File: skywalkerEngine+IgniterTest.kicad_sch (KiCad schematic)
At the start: 49 parts

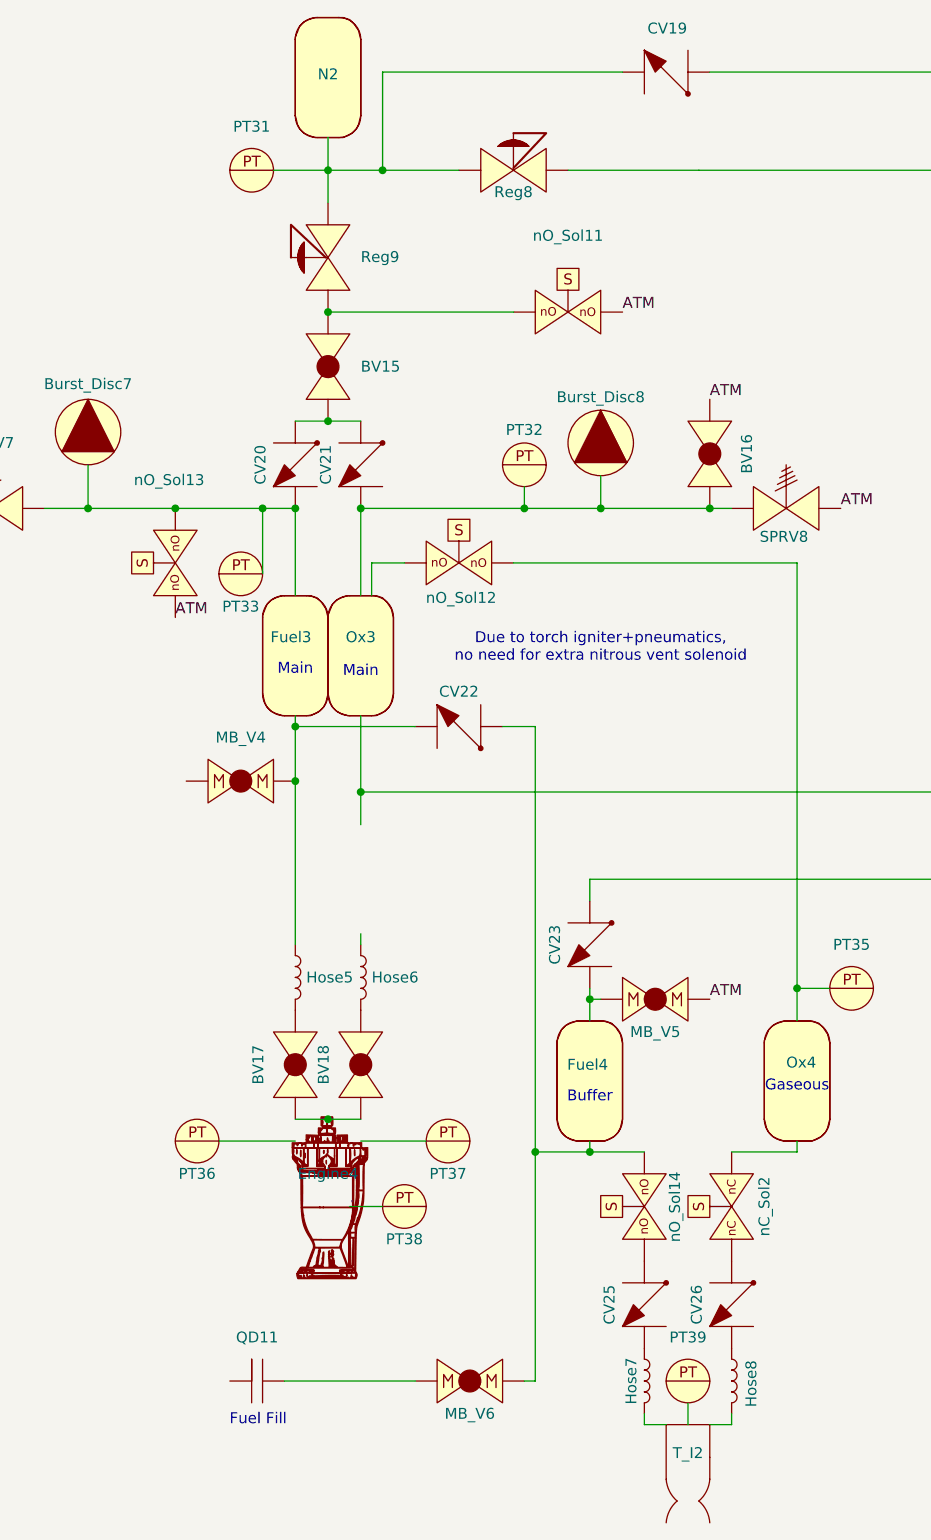
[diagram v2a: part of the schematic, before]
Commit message: Modified Hopper Eng test
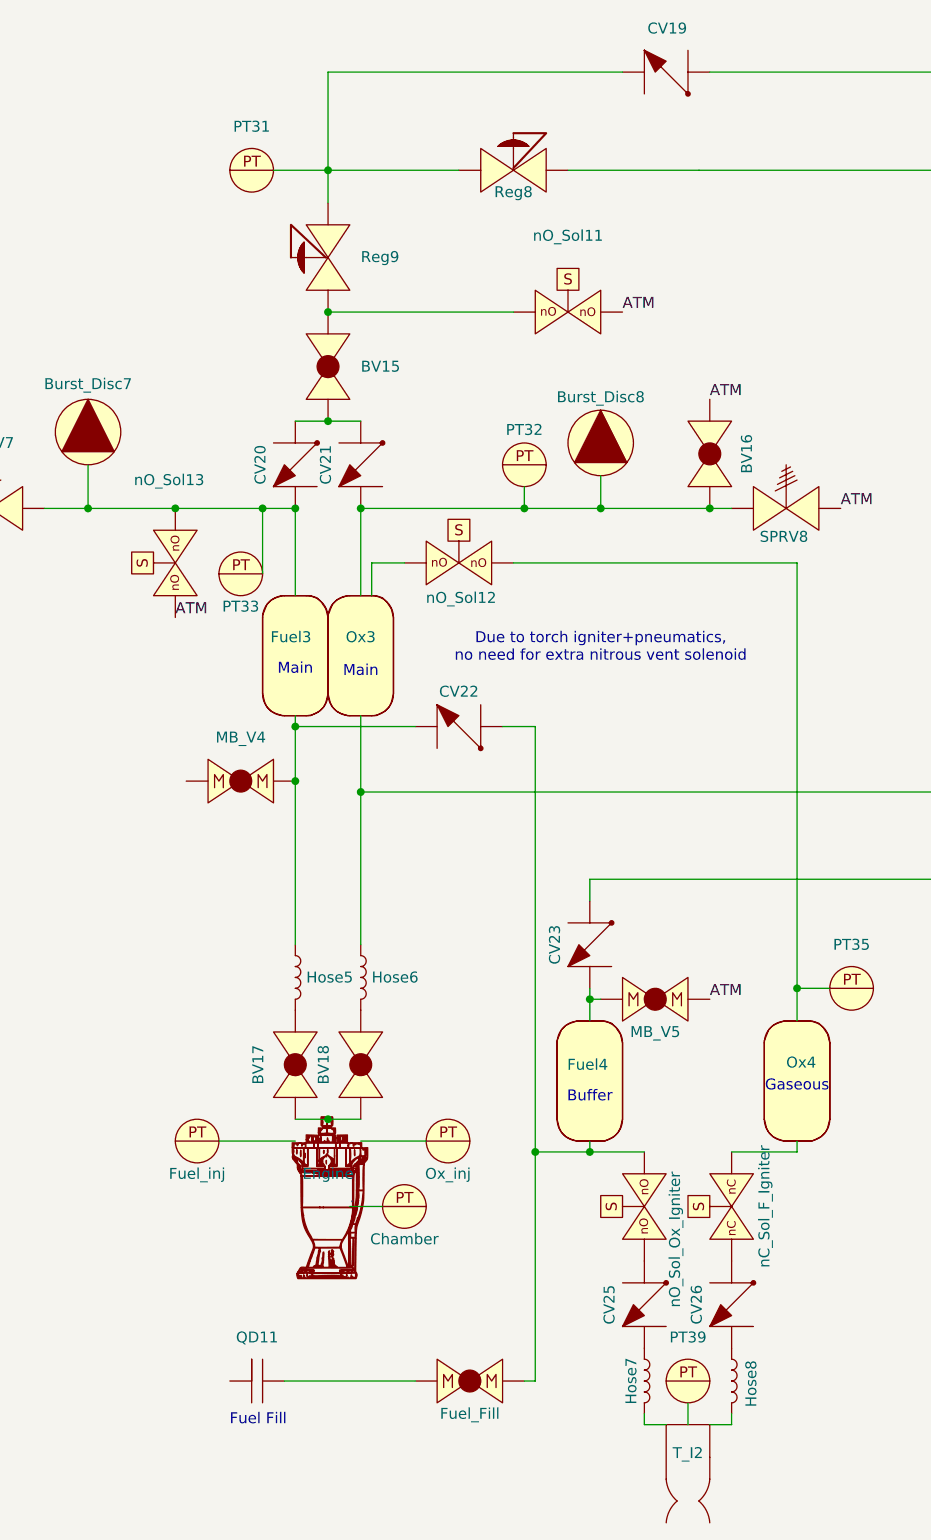
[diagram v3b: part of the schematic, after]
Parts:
- removed N2: ~, symbol PID_symbols:Tank
- renumbered PT38 to Chamber, Engine4 to Engine, MB_V6 to Fuel_Fill, PT36 to Fuel_inj, PT37 to Ox_inj, nC_Sol2 to nC_Sol_F_Igniter, nO_Sol14 to nO_Sol_Ox_Igniter
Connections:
- net at Fuel_inj.: now also Engine.
- net at Engine.: now also Ox_inj.; no longer Fuel_inj.
- net at CV25.: now also Hose7.1; no longer nO_Sol_Ox_Igniter.
- net at MB_V4.: now also CV22., Fuel3., Hose5.1
- net at QD9.: now also CV24.
- net at CV24.: now also Hose6.1, Ox3.; no longer QD9.
- net at PT31.: now also CV19., Reg8., Reg9.
- net at Ox_inj.: no longer Engine.
- new net: Burst_Disc7., CV20., Fuel3., PT33., SPRV7., nO_Sol13.
- new net: Ox4., PT35., nO_Sol12.
- new net: CV25., nO_Sol_Ox_Igniter.
- new net: CV23., PT34., Reg8.
- new net: CV23., Fuel4., MB_V5.
- new net: BV17., BV18., Engine.
- new net: BV16., Burst_Disc8., CV21., Ox3., PT32., SPRV8.
- new net: BV15., Reg9., nO_Sol11.
- now unconnected: Burst_Disc7., Burst_Disc8., PT32., PT33., PT34., PT35.
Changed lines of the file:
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@@
 	)
 	(junction
-		(at 71.12 38.1)
-		(diameter 0)
-		(color 0 0 0 0)
-	)
-	(junction
 		(at 119.38 133.35)
 		(diameter 0)
@@
 	(wire
 		(pts
-			(xy 71.12 26.67) (xy 99.06 26.67)
+			(xy 64.77 26.67) (xy 99.06 26.67)
 		)
 		(stroke
@@
 	(wire
 		(pts
-			(xy 71.12 38.1) (xy 71.12 26.67)
+			(xy 64.77 38.1) (xy 64.77 26.67)
 		)
 		(stroke
@@
 	(wire
 		(pts
-			(xy 68.58 128.27) (xy 68.58 127)
-		)
-		(stroke
-			(width 0)
-			(type default)
-		)
-	)
-	(wire
-		(pts
 			(xy 85.09 102.87) (xy 88.9 102.87)
 		)
@@
 	(wire
 		(pts
-			(xy 71.12 38.1) (xy 80.01 38.1)
-		)
-		(stroke
-			(width 0)
-			(type default)
-		)
-	)
-	(wire
-		(pts
 			(xy 69.85 83.82) (xy 69.85 87.63)
 		)
@@
 	(wire
 		(pts
-			(xy 68.58 110.49) (xy 68.58 114.3)
-		)
-		(stroke
-			(width 0)
-			(type default)
-		)
-	)
-	(wire
-		(pts
 			(xy 60.96 148.59) (xy 64.77 148.59)
 		)
@@
 	(wire
 		(pts
-			(xy 64.77 38.1) (xy 71.12 38.1)
+			(xy 64.77 38.1) (xy 80.01 38.1)
 		)
 		(stroke
@@
 	(wire
 		(pts
-			(xy 64.77 38.1) (xy 64.77 34.29)
+			(xy 87.63 77.47) (xy 96.52 77.47)
 		)
 		(stroke
@@
 	(wire
 		(pts
-			(xy 87.63 77.47) (xy 96.52 77.47)
+			(xy 68.58 110.49) (xy 68.58 128.27)
 		)
 		(stroke
@@
 		(on_board yes)
 		(dnp no)
-		(property "Reference" "PT36"
+		(property "Reference" "Fuel_inj"
 			(at 49.53 154.94 0)
 			(effects
@@
 			(project "P_IDs"
 				(path "/045f1f05-3134-4b6d-91b6-463031104f1e/e56eb7fc-ceaa-4516-b7d6-446a7aeba6c0"
-					(reference "PT36")
+					(reference "Fuel_inj")
 					(unit 1)
 				)
@@
 		(on_board yes)
 		(dnp no)
-		(property "Reference" "PT38"
+		(property "Reference" "Chamber"
 			(at 73.66 162.56 0)
 			(effects
@@
 			(project "P_IDs"
 				(path "/045f1f05-3134-4b6d-91b6-463031104f1e/e56eb7fc-ceaa-4516-b7d6-446a7aeba6c0"
-					(reference "PT38")
+					(reference "Chamber")
 					(unit 1)
 				)
@@
 		(on_board yes)
 		(dnp no)
-		(property "Reference" "MB_V6"
+		(property "Reference" "Fuel_Fill"
 			(at 81.28 182.88 0)
 			(effects
@@
 			(project "P_IDs"
 				(path "/045f1f05-3134-4b6d-91b6-463031104f1e/e56eb7fc-ceaa-4516-b7d6-446a7aeba6c0"
-					(reference "MB_V6")
+					(reference "Fuel_Fill")
 					(unit 1)
 				)
@@
 		(on_board yes)
 		(dnp no)
-		(property "Reference" "nO_Sol14"
+		(property "Reference" "nO_Sol_Ox_Igniter"
 			(at 105.156 154.686 0)
 			(effects
@@
 			(project "P_IDs"
 				(path "/045f1f05-3134-4b6d-91b6-463031104f1e/e56eb7fc-ceaa-4516-b7d6-446a7aeba6c0"
-					(reference "nO_Sol14")
+					(reference "nO_Sol_Ox_Igniter")
 					(unit 1)
 				)
@@
 		(on_board yes)
 		(dnp no)
-		(property "Reference" "nC_Sol2"
+		(property "Reference" "nC_Sol_F_Igniter"
 			(at 115.57 158.75 0)
 			(effects
@@
 			(project "P_IDs"
 				(path "/045f1f05-3134-4b6d-91b6-463031104f1e/e56eb7fc-ceaa-4516-b7d6-446a7aeba6c0"
-					(reference "nC_Sol2")
+					(reference "nC_Sol_F_Igniter")
 					(unit 1)
 				)
@@
 		(on_board yes)
 		(dnp no)
-		(property "Reference" "Engine4"
+		(property "Reference" "Engine"
 			(at 64.77 154.94 0)
 			(effects
@@
 			(project "P_IDs"
 				(path "/045f1f05-3134-4b6d-91b6-463031104f1e/e56eb7fc-ceaa-4516-b7d6-446a7aeba6c0"
-					(reference "Engine4")
+					(reference "Engine")
 					(unit 1)
 				)
@@
 		(on_board yes)
 		(dnp no)
-		(property "Reference" "PT37"
+		(property "Reference" "Ox_inj"
 			(at 78.74 154.94 0)
 			(effects
@@
 			(project "P_IDs"
 				(path "/045f1f05-3134-4b6d-91b6-463031104f1e/e56eb7fc-ceaa-4516-b7d6-446a7aeba6c0"
-					(reference "PT37")
+					(reference "Ox_inj")
 					(unit 1)
 				)
@@
 					(unit 1)
 				)
-			)
-		)
-	)
-	(symbol
-		(lib_name "PID_symbols:Tank")
-		(lib_id "PID_symbols:Tank")
-		(at 63.5 31.75 0)
-		(unit 1)
-		(exclude_from_sim no)
-		(in_bom yes)
-		(on_board yes)
-		(dnp no)
-		(property "Reference" "N2"
-			(at 64.77 26.924 0)
-			(effects
-				(font
-					(size 1.27 1.27)
-				)
-			)
-		)
-		(property "Value" "~"
-			(at 63.5 31.75 0)
-			(effects
-				(font
-					(size 1.27 1.27)
-				)
-			)
-		)
-		(property "Footprint" ""
-			(at 63.5 31.75 0)
-			(effects
-				(font
-					(size 1.27 1.27)
-				)
-				(hide yes)
-			)
-		)
-		(property "Datasheet" ""
-			(at 63.5 31.75 0)
-			(effects
-				(font
-					(size 1.27 1.27)
-				)
-				(hide yes)
-			)
-		)
-		(property "Description" ""
-			(at 63.5 31.75 0)
-			(effects
-				(font
-					(size 1.27 1.27)
-				)
-				(hide yes)
-			)
-		)
-		(pin ""
-		)
-		(pin ""
-		)
-		(instances
-			(project "P_IDs"
-				(path "/045f1f05-3134-4b6d-91b6-463031104f1e/e56eb7fc-ceaa-4516-b7d6-446a7aeba6c0"
-					(reference "N2")
-					(unit 1)
-				)

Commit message: overwrite
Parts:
- removed BV15: ~, symbol PID_symbols:Ball_Valve
- removed CV24: ~, symbol PID_symbols:Check_Valve
- removed QD10, QD9: ~, symbol PID_symbols:Quick_Disconnect
- added CV?: ~, symbol PID_symbols:Check_Valve
- added Hose?: ~, symbol Device:Hose
- added N2_Bottl;e, Ox_Bottle: ~, symbol PID_symbols:Tank
- added N2_Press, N2_Press?: ~, symbol PID_symbols:Ball_Valve
- added PT?: ~, symbol PID_symbols:Pressure_Transducer
- added nO_Sol?: ~, symbol PID_symbols:Normally Open Solenoid
- renumbered PT33 to Fuel_Tank, PT31 to N2_Hose, PT34 to N2_Pn, PT35 to Ox_Buffer, PT32 to Ox_Tank
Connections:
- net ATM: now also nO_Sol?.
- net at Fuel_inj.: now also Engine.
- net at Engine.: now also Ox_inj.; no longer Fuel_inj.
- net at CV25.: now also Hose7.1; no longer nO_Sol_Ox_Igniter.
- net at CV20., CV21.: now also Reg9., nO_Sol11.
- net at MB_V4.: now also CV22., Fuel3., Hose5.1
- net at Reg9.: now also CV19., N2_Hose., Reg8.; no longer nO_Sol11.
- net at Hose6.1, Ox3.: now also CV?.
- net at Ox_inj.: no longer Engine.
- net at CV19.: now also N2_Press.
- new net: Burst_Disc7., CV20., Fuel3., Fuel_Tank., SPRV7., nO_Sol13.
- new net: Ox4., Ox_Buffer., nO_Sol12.
- new net: CV25., nO_Sol_Ox_Igniter.
- new net: CV23., N2_Pn., Reg8.
- new net: CV23., Fuel4., MB_V5.
- new net: Hose?.1, N2_Press., PT?.
- new net: BV17., BV18., Engine.
- new net: BV16., Burst_Disc8., CV21., Ox3., Ox_Tank., SPRV8., nO_Sol?.
- new net: N2_Press?., Ox_Bottle.
- new net: Hose?.2, N2_Bottl;e.
- new net: CV?., N2_Press?.
- now unconnected: Burst_Disc7., Burst_Disc8., Fuel_Tank., N2_Pn., Ox_Buffer., Ox_Tank.
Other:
- note removed: "Nitrous Fill"
- moved on the sheet: BV16, Fuel_Tank, SPRV8

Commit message: no message
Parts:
- removed BV16, BV17, BV18, N2_Press, N2_Press?: ~, symbol PID_symbols:Ball_Valve
- removed Burst_Disc7, Burst_Disc8: ~, symbol PID_symbols:Burst_Disc
- removed CV19, CV20, CV21, CV22, CV23, CV25, CV26, CV?: ~, symbol PID_symbols:Check_Valve
- removed Chamber, Fuel_Tank, Fuel_inj, N2_Hose, N2_Pn, Ox_Buffer, Ox_Tank, Ox_inj, PT39, PT?: ~, symbol PID_symbols:Pressure_Transducer
- removed Engine: ~, symbol PID_symbols:Engine
- removed Fuel3, Fuel4, N2_Bottl;e, Ox3, Ox4, Ox_Bottle: ~, symbol PID_symbols:Tank
- removed Fuel_Fill, MB_V4, MB_V5: ~, symbol PID_symbols:MBallValve
- removed Hose5, Hose6, Hose7, Hose8, Hose?: ~, symbol Device:Hose
- removed QD11: ~, symbol PID_symbols:Quick_Disconnect
- removed Reg8, Reg9: ~, symbol PID_symbols:Pressure_Regulator
- removed SPRV7, SPRV8: ~, symbol PID_symbols:SPRV
- removed T_I2: ~, symbol Analog_ADC:Torch_Igniter
- removed nC_Sol_F_Igniter: ~, symbol PID_symbols:Normally_Closed_Solenoid
- removed nO_Sol11, nO_Sol12, nO_Sol13, nO_Sol_Ox_Igniter: ~, symbol PID_symbols:Solenoid
- removed nO_Sol?: ~, symbol PID_symbols:Normally Open Solenoid
- added BV? (x6): ~, symbol PID_symbols:Ball_Valve
- added Burst_Disc?: ~, symbol PID_symbols:Burst_Disc
- added CV? (x3): ~, symbol PID_symbols:Check_Valve
- added Engine?: ~, symbol PID_symbols:Engine
- added Hose? (x2): ~, symbol Device:Hose
- added PT? (x7): ~, symbol PID_symbols:Pressure_Transducer
- added Pmatic_B_Valve?: ~, symbol PID_symbols:Pneumatic_Rotary_Ball_Valve
- added Reg? (x2): ~, symbol PID_symbols:Pressure_Regulator
- added SPRV?: ~, symbol PID_symbols:SPRV
- added T? (x6): ~, symbol PID_symbols:Tank
- added nO_Sol? (x3): ~, symbol PID_symbols:Solenoid
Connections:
- net .: now also PT?.
- new net: BV?., Engine?., PT?. (x2)
- new net: Reg?., T?.
- new net: BV?., Pmatic_B_Valve?.
- new net: BV?., CV?., PT?., T?.
- new net: CV?., Hose?.2
- new net: Hose?.1, T?.
- new net: BV?., Burst_Disc?., CV?., CV?., SPRV?.
- new net: BV?., Reg?.
- new net: T?., nO_Sol?.
- new net: BV?., CV?., T?., nO_Sol?.
- new net: BV?., T?.
- new net: Hose?.2, PT?., Reg?., Reg?.
- new net: PT?., Pmatic_B_Valve?., T?.
- new net: BV?., Hose?.1
- new net: BV?., CV?., nO_Sol?.
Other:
- note removed: "Buffer"
- note removed: "Due to torch igniter+pneumatics, no need for extra nitrous vent solenoid"
- note removed: "Fuel Fill"
- note removed: "Gaseous"
- note removed: "Main"

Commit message: no message
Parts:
- removed Pmatic_B_Valve?: ~, symbol PID_symbols:Pneumatic_Rotary_Ball_Valve
- added CV? (x3): ~, symbol PID_symbols:Check_Valve
- added Hose? (x2): ~, symbol Device:Hose
- added MB_V? (x2): ~, symbol PID_symbols:MBallValve
- added PT?: ~, symbol PID_symbols:Pressure_Transducer
- added QD?: ~, symbol PID_symbols:Quick_Disconnect
- added T_I?: ~, symbol Analog_ADC:Torch_Igniter
- added nC_Sol?: ~, symbol PID_symbols:Normally_Closed_Solenoid
- added nO_Sol?: ~, symbol PID_symbols:Normally Open Solenoid
- gave numbers to parts that had none: 2
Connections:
- net at Engine?.: now also BV?., PT?.
- net at Eth_Buff.: now also BV?., PT?., T?., MB_V?., nO_Sol?.
- net at Reg?.: now also CV?.; no longer Eth_Buff.
- net at T?.: now also Hose?.1
- net at nO_Sol?.: now also Ox_Buffer.
- net at BV?.: now also CV?., T?., nO_Sol?.
- net at T?.: now also BV?.
- net at BV?.: now also Hose?.1; no longer T?.
- net at PT?.: no longer T?.
- net at BV?.: now also CV?., nO_Sol?.
- new net: BV?., Engine?., PT?.
- new net: CV?., Eth_Buff., MB_V?.
- new net: CV?., nC_Sol?.
- new net: Ox_Buffer., nC_Sol?.
- new net: BV?., CV?., PT?., T?.
- new net: BV?., Burst_Disc?., CV?., CV?., SPRV?.
- new net: CV?., Hose?.1
- new net: Hose?.2, T_I?.
- new net: CV?., nO_Sol?.
- new net: CV?., Hose?.2
- new net: MB_V?., QD?.
- new net: Hose?.1, T_I?.
- now unconnected: Burst_Disc?., PT?., PT?., PT?., SPRV?., nO_Sol?., nO_Sol?.
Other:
- moved on the sheet: BV?, Engine?, Eth_Buff, Ox_Buffer, PT?

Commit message: no message
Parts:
- added CV?: ~, symbol PID_symbols:Check_Valve
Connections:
- net at Engine?.: now also BV?., PT?.
- net at nC_Sol?.: now also Ox_Buffer.; no longer CV?.
- net at Ox_Buffer.: now also nO_Sol?.; no longer nC_Sol?.
- net at T?.: now also Hose?.1
- net at BV?.: now also CV?., T?., nO_Sol?.
- net at T?.: now also BV?.
- net at BV?.: now also Hose?.1; no longer T?.
- net at QD?.: now also MB_V?.
- net at BV?.: now also CV?., nO_Sol?.
- new net: CV?., Eth_Buff., MB_V?., nO_Sol?.
- new net: BV?., CV?., PT?., T?. (x2)
- new net: BV?., Engine?., PT?.
- new net: CV?., Eth_Buff., MB_V?.
- new net: CV?., nC_Sol?.
- new net: BV?., Burst_Disc?., CV?., CV?., SPRV?.
- now unconnected: Burst_Disc?., MB_V?., PT?., PT?., PT?., PT?., SPRV?., T?., nO_Sol?., nO_Sol?.
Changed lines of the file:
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@@
+	(wire
+		(pts
+			(xy 186.69 91.44) (xy 186.69 102.87)
+		)
+		(stroke
+			(width 0.635)
+			(type default)
+		)
+	)
 	(wire
 		(pts
@@
 	(wire
 		(pts
-			(xy 186.69 73.66) (xy 186.69 102.87)
+			(xy 186.69 73.66) (xy 186.69 81.28)
 		)
 		(stroke
@@
 		)
 	)
+	(symbol
+		(lib_name "Check_Valve_3")
+		(lib_id "PID_symbols:Check_Valve")
+		(at 186.69 88.9 90)
+		(unit 1)
+		(exclude_from_sim no)
+		(in_bom yes)
+		(on_board yes)
+		(dnp no)
+		(fields_autoplaced yes)
+		(property "Reference" "CV?"
+			(at 190.5 85.8519 90)
+			(effects
+				(font
+					(size 1.27 1.27)
+				)
+				(justify right)
+			)
+		)
+		(property "Value" "~"
+			(at 190.5 87.757 90)
+			(effects
+				(font
+					(size 1.27 1.27)
+				)
+				(justify right)
+			)
+		)
+		(property "Footprint" ""
+			(at 186.69 88.9 0)
+			(effects
+				(font
+					(size 1.27 1.27)
+				)
+				(hide yes)
+			)
+		)
+		(property "Datasheet" ""
+			(at 186.69 88.9 0)
+			(effects
+				(font
+					(size 1.27 1.27)
+				)
+				(hide yes)
+			)
+		)
+		(property "Description" ""
+			(at 186.69 88.9 0)
+			(effects
+				(font
+					(size 1.27 1.27)
+				)
+				(hide yes)
+			)
+		)
+		(pin ""
+		)
+		(pin ""
+		)
+		(instances
+			(project ""
+				(path "/045f1f05-3134-4b6d-91b6-463031104f1e/e56eb7fc-ceaa-4516-b7d6-446a7aeba6c0"
+					(reference "CV?")
+					(unit 1)
+				)
+			)
+		)
+	)

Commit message: no message
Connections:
- net at Engine?.: now also BV?., PT?.
- net at nC_Sol?.: now also Ox_Buffer.; no longer CV?.
- net at Ox_Buffer.: now also nO_Sol?.; no longer nC_Sol?.
- net at T?.: now also Hose?.1
- net at BV?.: now also CV?., T?., nO_Sol?.
- net at T?.: now also BV?.
- net at BV?.: now also Hose?.1; no longer T?.
- net at QD?.: now also MB_V?.
- net at BV?.: now also CV?., nO_Sol?.
- new net: CV?., Eth_Buff., MB_V?., nO_Sol?.
- new net: BV?., CV?., PT?., T?. (x2)
- new net: BV?., Engine?., PT?.
- new net: CV?., Eth_Buff., MB_V?.
- new net: CV?., nC_Sol?.
- new net: BV?., Burst_Disc?., CV?., CV?., SPRV?.
- now unconnected: Burst_Disc?., MB_V?., PT?., PT?., PT?., PT?., SPRV?., T?., nO_Sol?., nO_Sol?.
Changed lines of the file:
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@@
 	)
 	(symbol
-		(lib_name "PID_symbols:Ball_Valve")
 		(lib_id "PID_symbols:Ball_Valve")
 		(at 143.51 110.49 270)
@@
 	)
 	(symbol
-		(lib_name "PID_symbols:Check_Valve")
 		(lib_id "PID_symbols:Check_Valve")
 		(at 93.98 107.95 0)
@@
 	)
 	(symbol
-		(lib_name "PID_symbols:Tank")
 		(lib_id "PID_symbols:Tank")
 		(at 124.46 30.48 0)
@@
 	)
 	(symbol
-		(lib_name "PID_symbols:Ball_Valve")
 		(lib_id "PID_symbols:Ball_Valve")
 		(at 130.81 118.11 90)
@@
 	)
 	(symbol
-		(lib_name "PID_symbols:Pressure_Transducer")
 		(lib_id "PID_symbols:Pressure_Transducer")
 		(at 125.73 132.08 0)
@@
 	)
 	(symbol
-		(lib_name "PID_symbols:Ball_Valve")
 		(lib_id "PID_symbols:Ball_Valve")
 		(at 125.73 63.5 270)
@@
 	)
 	(symbol
-		(lib_name "PID_symbols:Pressure_Transducer")
 		(lib_id "PID_symbols:Pressure_Transducer")
 		(at 125.73 125.73 0)
@@
 	)
 	(symbol
-		(lib_name "PID_symbols:Pressure_Transducer")
 		(lib_id "PID_symbols:Pressure_Transducer")
 		(at 114.3 119.38 0)
@@
 	)
 	(symbol
-		(lib_name "PID_symbols:Solenoid")
 		(lib_id "PID_symbols:Solenoid")
 		(at 100.33 127 90)
@@
 	)
 	(symbol
-		(lib_name "PID_symbols:Check_Valve")
 		(lib_id "PID_symbols:Check_Valve")
 		(at 203.2 118.11 270)
@@
 	)
 	(symbol
-		(lib_name "PID_symbols:Pressure_Transducer")
 		(lib_id "PID_symbols:Pressure_Transducer")
 		(at 147.32 123.19 0)
@@
 	)
 	(symbol
-		(lib_name "PID_symbols:Ball_Valve")
 		(lib_id "PID_symbols:Ball_Valve")
 		(at 107.95 87.63 0)
@@
 	)
 	(symbol
-		(lib_name "PID_symbols:Tank")
 		(lib_id "PID_symbols:Tank")
 		(at 76.2 68.58 0)
@@
 	)
 	(symbol
-		(lib_name "PID_symbols:Solenoid")
 		(lib_id "PID_symbols:Solenoid")
 		(at 95.25 87.63 0)
@@
 	)
 	(symbol
-		(lib_name "PID_symbols:Tank")
 		(lib_id "PID_symbols:Tank")
 		(at 104.14 102.87 0)
@@
 	)
 	(symbol
-		(lib_name "PID_symbols:Tank")
 		(lib_id "PID_symbols:Tank")
 		(at 161.29 62.23 0)
@@
 	)
 	(symbol
-		(lib_name "PID_symbols:Ball_Valve")
 		(lib_id "PID_symbols:Ball_Valve")
 		(at 77.47 73.66 270)
@@
 	)
 	(symbol
-		(lib_name "PID_symbols:Pressure_Transducer")
 		(lib_id "PID_symbols:Pressure_Transducer")
 		(at 137.16 118.11 0)
@@
 	)
 	(symbol
-		(lib_name "PID_symbols:Check_Valve")
 		(lib_id "PID_symbols:Check_Valve")
 		(at 105.41 76.2 270)
@@
 	)
 	(symbol
-		(lib_name "PID_symbols:Ball_Valve")
 		(lib_id "PID_symbols:Ball_Valve")
 		(at 146.05 88.9 0)
@@
 	)
 	(symbol
-		(lib_name "PID_symbols:Pressure_Transducer")
 		(lib_id "PID_symbols:Pressure_Transducer")
 		(at 170.18 83.82 0)
@@
 	)
 	(symbol
-		(lib_name "PID_symbols:Check_Valve")
 		(lib_id "PID_symbols:Check_Valve")
 		(at 135.89 73.66 0)
@@
 	)
 	(symbol
-		(lib_name "PID_symbols:Solenoid")
 		(lib_id "PID_symbols:Solenoid")
 		(at 146.05 82.55 0)
@@
 	)
 	(symbol
-		(lib_name "PID_symbols:Pressure_Transducer")
 		(lib_id "PID_symbols:Pressure_Transducer")
 		(at 106.68 49.53 0)
